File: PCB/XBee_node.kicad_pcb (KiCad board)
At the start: 2 copper layers, 70 x 55 mm, 23 parts, among them J1 conn_2x16, U1 Nano, U2 MCP2515, U3 MCP2551, U4 PushButton, U5 XBee_adapter, U6 DIPSwitch_12, U7 DIPSwitch_3, Y1 16MHz

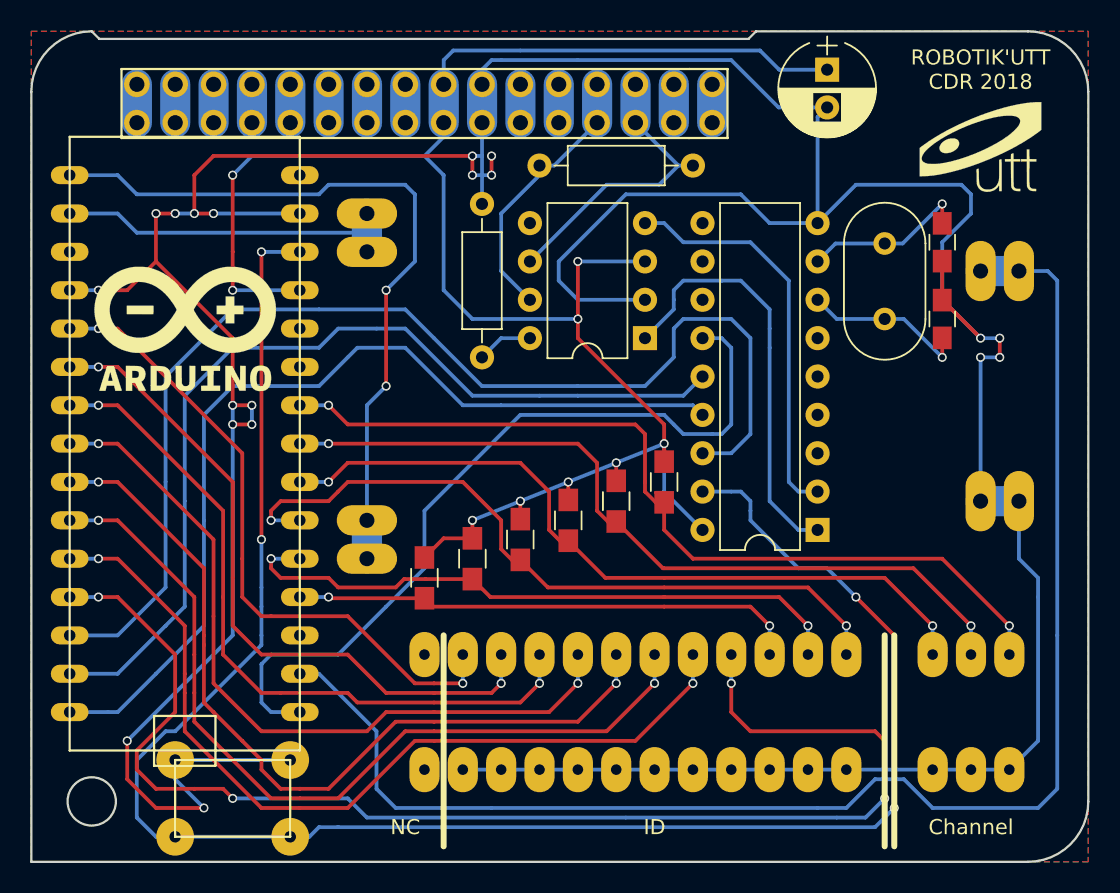
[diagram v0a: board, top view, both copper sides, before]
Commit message: reduced ID to implement SoftwareSerial
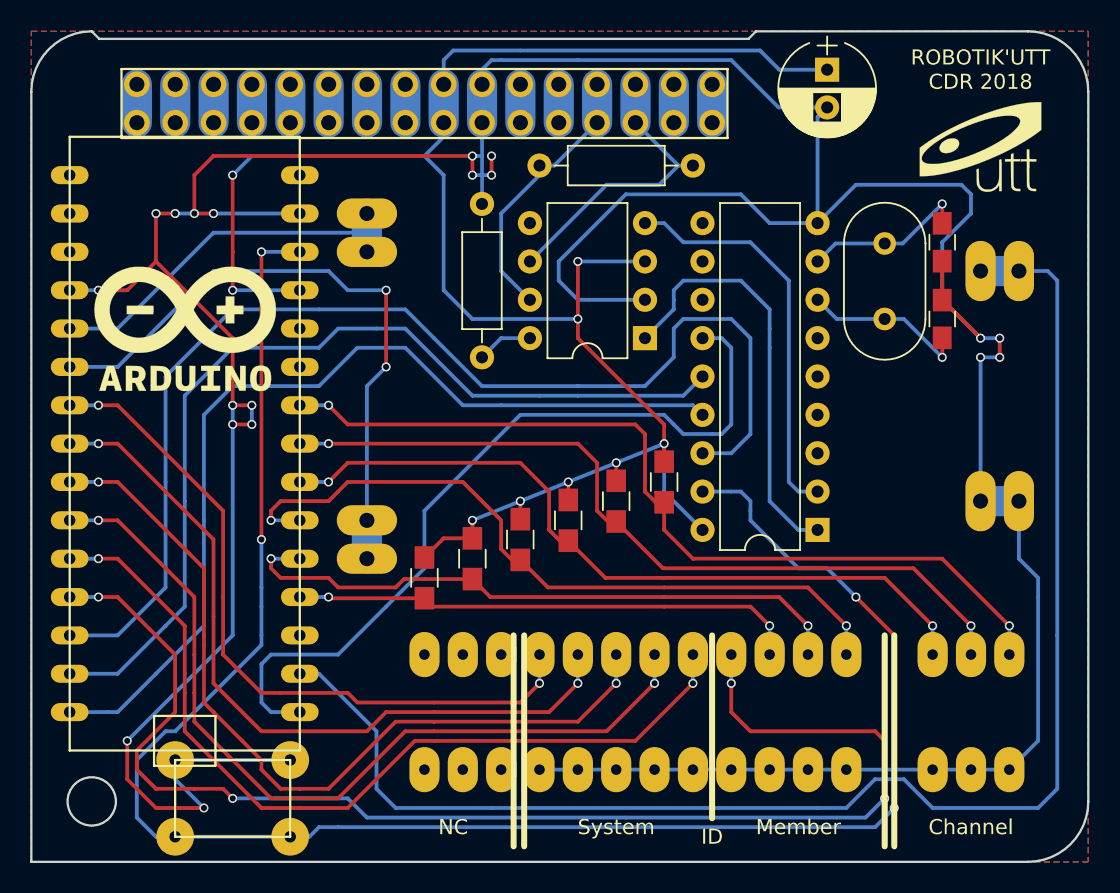
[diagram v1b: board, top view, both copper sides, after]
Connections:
- U1 pad 1: /TX -> Net-(U1-Pad1)
- U1 pad 2: /RX -> Net-(U1-Pad2)
- U1 pad 5: /D2 -> /RX
- U1 pad 6: /D3 -> /TX
- U6 pad 2: /GNDL -> Net-(U6-Pad2)
- U6 pad 22: /D3 -> Net-(U6-Pad22)
- U6 pad 23: /D2 -> Net-(U6-Pad23)
- U6 pad 3: /GNDL -> Net-(U6-Pad3)
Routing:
- net /D3: track 45.9 -> 0.00 mm, vias 2 -> 0
- net /D2: track 43.3 -> 0.00 mm, vias 2 -> 0
- net /TX: track 49.4 -> 42.4 mm
- net /GNDL: track 274.4 -> 269.3 mm
- net /RX: track 22.8 -> 24.9 mm
- net Net-(U6-Pad22): track 0.00 -> 0.64 mm
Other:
- board text added: "Member"
- board text added: "System"
